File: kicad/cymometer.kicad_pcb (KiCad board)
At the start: 2 copper layers, 135.4 x 62 mm, 45 parts, among them IC1 74150, IC2 ATTINY2313-P, P1 BNC, P2 CONN_3X2, P3 CONN_10, P4 CONN_2, Q1 BC550, U1 74LS196, U2 74LS196, U3 74LS90, U4 74LS90, U5 7400, U6 74LS173, U7 7805, X1 127kHz

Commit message: Add new circuit
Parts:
- removed C13: CP1, Capacitors_ThroughHole:C_Radial_D8_L11.5_P3.5
- removed C14: CTRIM, Potentiometers:Potentiometer_Trimmer-Piher_PT15-V12-5_horizontal
- removed IC2: ATTINY2313-P, Housings_DIP:DIP-20_W7.62mm_LongPads
- removed U2: 74LS196, Housings_DIP:DIP-14_W7.62mm_LongPads
- removed U3, U4: 74LS90, Housings_DIP:DIP-14_W7.62mm_LongPads
- removed U5: 7400, Housings_DIP:DIP-14_W7.62mm_LongPads
- removed U6: 74LS173, Housings_DIP:DIP-16_W7.62mm_LongPads
- removed U7: 7805, Power_Integrations:TO-220
- added DD1: к531ие14, Housings_DIP:DIP-14_W7.62mm_LongPads, F.Cu at (84.1, 33.0)
- added DD2: к531ие14, Housings_DIP:DIP-14_W7.62mm_LongPads, F.Cu at (83.8, 68.1)
- added DD3: к155ла3, Housings_DIP:DIP-14_W7.62mm_LongPads, F.Cu at (38.5, 31.8)
- added DD4: кр1533кп7, Housings_DIP:DIP-16_W7.62mm_LongPads, F.Cu at (83.8, 51.0)
- added DD5: к155ир15, Housings_DIP:DIP-16_W7.62mm_LongPads, F.Cu at (56.9, 68.1)
- C1: value C -> 0.22; footprint Capacitors_ThroughHole:C_Disc_D12_P7.75 -> Capacitors_ThroughHole:C_Rect_L7_W2.5_P5
- C10, C11, C12, C7, C8, C9: value C -> 0.1; footprint Capacitors_ThroughHole:C_Disc_D12_P7.75 -> capacitors:C_Rect_L7_W2.5_P5
- C15: value C -> CTRIM; footprint Capacitors_ThroughHole:C_Disc_D12_P7.75 -> Potentiometers:Potentiometer_Trimmer-Piher_PT15-V12-5_horizontal
- C16: footprint Capacitors_ThroughHole:C_Disc_D12_P7.75 -> Capacitors_ThroughHole:C_Rect_L7_W2_P5
- C17: value CP1 -> C; footprint Capacitors_ThroughHole:C_Radial_D8_L21_P3.8 -> Capacitors_ThroughHole:C_Rect_L7_W2_P5
- C2: value C -> 100.0; footprint Capacitors_ThroughHole:C_Radial_D8_L13_P3.8 -> Capacitors_ThroughHole:C_Radial_D6.3_L11.2_P2.5
- C3: value C -> 680; footprint Capacitors_ThroughHole:C_Rect_L13_W4_P10 -> Capacitors_ThroughHole:C_Rect_L7_W3.5_P5
- C4: value CP1 -> 22.0; footprint Capacitors_ThroughHole:C_Radial_D8_L13_P3.8 -> Capacitors_ThroughHole:C_Radial_D6.3_L11.2_P2.5
- C5: value C -> 470.0; footprint Capacitors_ThroughHole:C_Disc_D12_P7.75 -> Capacitors_ThroughHole:C_Radial_D8_L21_P3.8
- C6: value C -> 100.0; footprint Capacitors_ThroughHole:C_Disc_D12_P7.75 -> Capacitors_ThroughHole:C_Radial_D6.3_L11.2_P2.5
- D1: value DIODE -> КД503А
- IC1: value 74150 -> ATTINY2313-P; footprint Housings_DIP:DIP-24_W15.24mm_LongPads -> Housings_DIP:DIP-20_W7.62mm_LongPads
- P1: footprint Connect:bornier2 -> Pin_Headers:Pin_Header_Straight_1x02
- P2: value CONN_3X2 -> CONN_2; footprint Socket_Strips:Socket_Strip_Straight_2x03 -> Pin_Headers:Pin_Header_Straight_1x02
- P3: value CONN_10 -> CONN_3X2; footprint Socket_Strips:Socket_Strip_Straight_1x10 -> Pin_Headers:Pin_Header_Straight_2x03
- P4: value CONN_2 -> CONN_12; footprint Connect:bornier2 -> Pin_Headers:Pin_Header_Straight_1x12
- R1: value R -> 10k
- R10: value R -> 510
- R2: value R -> 1k; footprint Resistors_ThroughHole:Resistor_Horizontal_RM25mm -> Resistors_ThroughHole:Resistor_Horizontal_RM10mm
- R3: value R -> 150k
- R4: value R -> 360
- R5: value R -> 100
- R6: value R -> 1k
- R7, R8: value R -> 2.2k
- R9: value R -> 47k
- RV1: value POT -> 1k
- U1: value 74LS196 -> 7805; footprint Housings_DIP:DIP-14_W7.62mm_LongPads -> Power_Integrations:TO-220
- X1: value 127kHz -> 16.000
- moved C8 97.4 mm to (35.1, 27.9), turned to 270 degrees
- moved P1 77.5 mm to (31.2, 71.4)
- moved C17 69.4 mm to (83.9, 23.7), turned to 270 degrees
- moved C1 69.2 mm to (31.4, 67.1), turned to 90 degrees
- moved D2 67.6 mm to (102.9, 80.0), turned to 0 degrees
- moved X1 61.6 mm to (75.2, 24.4), turned to 180 degrees
- moved P3 60.1 mm to (111.0, 26.9), turned to 0 degrees
- moved C16 59.2 mm to (66.3, 23.6), turned to 270 degrees
- moved C11 56.8 mm to (80.0, 78.5)
- moved C7 55.1 mm to (59.9, 71.9), turned to 270 degrees
- moved C5 51.3 mm to (104.3, 70.4), turned to 180 degrees
- moved C12 49.0 mm to (100.5, 36.4), turned to 180 degrees
- moved U1 48.6 mm to (95.2, 79.0)
- moved C15 44.7 mm to (102.2, 32.1), turned to 90 degrees
- moved IC1 43.2 mm to (96.7, 39.8), turned to 0 degrees
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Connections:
- C10 pad 1: +5V -> VCC
- C11 pad 1: +5V -> VCC
- C12 pad 1: +5V -> VCC
- C15 pad 1: Net-(C14-Pad1) -> Net-(C15-Pad1)
- C15 pad 2: GND -> Net-(C15-Pad2)
- C16 pad 1: Net-(C14-Pad2) -> Net-(C15-Pad1)
- C17 pad 1: Net-(C17-Pad1) -> Net-(C15-Pad2)
- C2 pad 1: GND -> Net-(C2-Pad1)
- C2 pad 2: Net-(C2-Pad2) -> GND
- C5 pad 1: +5V -> Net-(C5-Pad1)
- C6 pad 1: +5V -> VCC
- C7 pad 1: +5V -> GND
- C7 pad 2: GND -> VCC
- C8 pad 1: +5V -> VCC
- C9 pad 1: +5V -> VCC
- D2 pad 3: Net-(C17-Pad1) -> Net-(C5-Pad1)
- IC1 pad 10: Net-(IC1-Pad10) -> GND
- IC1 pad 12: GND -> Net-(IC1-Pad12)
- IC1 pad 20: Net-(IC1-Pad20) -> VCC
- IC1 pad 4: Net-(IC1-Pad4) -> Net-(C15-Pad1)
- IC1 pad 5: Net-(IC1-Pad5) -> Net-(C15-Pad2)
- IC1 pad 6: Net-(IC1-Pad6) -> Net-(DD5-Pad7)
- IC1 pad 7: Net-(IC1-Pad7) -> Net-(DD1-Pad13)
- IC1 pad 8: Net-(IC1-Pad8) -> Net-(DD2-Pad12)
- IC1 pad 9: GND -> Net-(IC1-Pad9)
- P2 pad 1: Net-(IC2-Pad18) -> Net-(D2-Pad4)
- P2 pad 2: +5V -> Net-(D2-Pad2)
- P3 pad 1: GND -> Net-(IC1-Pad18)
- P3 pad 2: +5V -> VCC
- P3 pad 3: Net-(IC2-Pad19) -> Net-(IC1-Pad19)
- P3 pad 4: Net-(IC2-Pad18) -> Net-(IC1-Pad17)
- P3 pad 5: Net-(IC2-Pad17) -> Net-(IC1-Pad1)
- P3 pad 6: Net-(IC2-Pad16) -> GND
- P4 pad 1: Net-(D2-Pad4) -> GND
- P4 pad 2: Net-(D2-Pad2) -> VCC
- Q1 pad 1: Net-(C2-Pad2) -> Net-(C2-Pad1)
- R1 pad 1: +5V -> Net-(C1-Pad2)
- R1 pad 2: Net-(R1-Pad2) -> Net-(D1-Pad2)
- R10 pad 1: +5V -> VCC
- R10 pad 2: Net-(R10-Pad2) -> Net-(DD1-Pad8)
- R2 pad 1: Net-(C1-Pad2) -> VCC
- R2 pad 2: Net-(D1-Pad2) -> Net-(DD1-Pad1)
- R3 pad 1: Net-(C2-Pad2) -> Net-(C2-Pad1)
- R5 pad 1: Net-(C2-Pad2) -> Net-(C2-Pad1)
- R5 pad 2: +5V -> VCC
- R7 pad 1: +5V -> VCC
- R8 pad 1: +5V -> VCC
- R9 pad 2: Net-(R10-Pad2) -> Net-(DD1-Pad8)
- RV1 pad 1: Net-(R6-Pad2) -> GND
- RV1 pad 3: GND -> Net-(R6-Pad2)
- U1 pad 1: Net-(R1-Pad2) -> Net-(C5-Pad1)
- U1 pad 2: Net-(IC1-Pad6) -> GND
- U1 pad 3: GND -> VCC
- X1 pad 1: Net-(C14-Pad2) -> Net-(C15-Pad2)
- X1 pad 2: Net-(C14-Pad1) -> Net-(C15-Pad1)
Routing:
- net +5V: track 391.6 -> 0.00 mm
- net VCC: track 0.00 -> 352.1 mm
- net GND: track 583.1 -> 420.9 mm
- net Net-(IC2-Pad7): track 148.2 -> 0.00 mm, vias 1 -> 0
- net Net-(IC2-Pad3): track 122.6 -> 0.00 mm, vias 2 -> 0
- net Net-(DD1-Pad12): track 0.00 -> 117.0 mm
- net Net-(IC1-Pad10): track 90.5 -> 0.00 mm
- net Net-(C15-Pad1): track 0.00 -> 88.7 mm
- net Net-(IC1-Pad7): track 86.6 -> 0.00 mm
- net Net-(IC1-Pad4): track 83.9 -> 0.00 mm
- net Net-(DD2-Pad12): track 0.00 -> 83.9 mm
- net Net-(IC1-Pad5): track 80.6 -> 0.00 mm, vias 1 -> 0
- net Net-(DD1-Pad13): track 0.00 -> 76.9 mm, vias 0 -> 1
- net Net-(U1-Pad13): track 69.7 -> 0.00 mm, vias 2 -> 0
- net Net-(IC1-Pad16): track 78.4 -> 9.45 mm
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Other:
- board size 135.4 x 62 mm -> 88.4 x 62 mm
- net class Default: clearance 0.7 -> 0.6
- rule trace_clearance: 0.7 -> 0.6
- board text added: "Cumometer"

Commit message: Add libraries
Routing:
- net Net-(DD1-Pad13): track 76.9 -> 59.7 mm
- net GND: track 420.9 -> 416.7 mm
- net Net-(DD3-Pad10): track 85.6 -> 81.6 mm
- net Net-(C15-Pad2): track 49.1 -> 46.8 mm
- net Net-(DD2-Pad2): track 29.6 -> 27.4 mm
- net Net-(DD5-Pad14): track 91.5 -> 93.6 mm
- net Net-(C15-Pad1): track 88.7 -> 86.8 mm
- net Net-(DD1-Pad12): track 117.0 -> 115.2 mm
- net Net-(DD2-Pad12): track 83.9 -> 85.7 mm
- net Net-(DD4-Pad9): track 26.7 -> 25.4 mm
- net Net-(DD2-Pad5): track 16.4 -> 15.2 mm
- net Net-(DD2-Pad9): track 27.2 -> 28.1 mm
- net Net-(DD1-Pad5): track 29.7 -> 28.8 mm
- net Net-(C5-Pad1): track 23.9 -> 23.2 mm
- net Net-(DD1-Pad9): track 14.1 -> 13.5 mm
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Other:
- board text added: "Cymometer"
- board text removed: "Cumometer"

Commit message: Add display board
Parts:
- added AFF1: 7SEGMENTS, cymometer:7segment_small, F.Cu at (155.0, 114.2)
- added AFF2: 7SEGMENTS, cymometer:7segment_small, F.Cu at (147.4, 114.2)
- added AFF3: 7SEGMENTS, cymometer:7segment_small, F.Cu at (139.8, 114.2)
- added AFF4: 7SEGMENTS, cymometer:7segment_small, F.Cu at (132.1, 114.2)
- added AFF5: 7SEGMENTS, cymometer:7segment_small, F.Cu at (124.5, 114.2)
- added AFF6: 7SEGMENTS, cymometer:7segment_small, F.Cu at (116.9, 114.2)
- added AFF7: 7SEGMENTS, cymometer:7segment_small, F.Cu at (109.3, 114.2)
- added AFF8: 7SEGMENTS, cymometer:7segment_small, F.Cu at (101.6, 114.3)
- added C13: C, cymometer:C_Rect_L7_W2.5_P5, B.Cu at (107.5, 132.2)
- added D4: LED, cymometer:LED, F.Cu at (96.5, 118.1)
- added D5: LED, cymometer:LED, F.Cu at (96.5, 110.5)
- added DD6: к155ид10, Housings_DIP:DIP-16_W7.62mm_LongPads, B.Cu at (111.0, 128.4)
- added DD7: 74HC595, Housings_DIP:DIP-16_W7.62mm_LongPads, B.Cu at (82.4, 128.4)
- added P5: CONN_12, Pin_Headers:Pin_Header_Straight_1x12, B.Cu at (168.6, 108.0)
- added R12: R, Resistors_ThroughHole:Resistor_Vertical_RM5mm, B.Cu at (104.1, 133.3)
- added R13: R, Resistors_ThroughHole:Resistor_Vertical_RM5mm, B.Cu at (83.8, 119.1)
- added R14: R, Resistors_ThroughHole:Resistor_Vertical_RM5mm, B.Cu at (87.1, 106.7)
- added R15: R, Resistors_ThroughHole:Resistor_Vertical_RM5mm, B.Cu at (86.4, 119.1)
- added R16: R, Resistors_ThroughHole:Resistor_Vertical_RM5mm, B.Cu at (89.0, 119.2)
- added R17: R, Resistors_ThroughHole:Resistor_Vertical_RM5mm, B.Cu at (91.6, 119.3)
- added R18: R, Resistors_ThroughHole:Resistor_Vertical_RM5mm, B.Cu at (87.1, 109.3)
- added R19: R, Resistors_ThroughHole:Resistor_Vertical_RM5mm, B.Cu at (87.0, 111.9)
- added SW1: SW_PUSH, Buttons_Switches_ThroughHole:SW_PUSH-12mm, F.Cu at (156.9, 131.0)
- added SW2: SW_PUSH, Buttons_Switches_ThroughHole:SW_PUSH-12mm, F.Cu at (140.1, 131.1)
- added SW3: SPST, Buttons_Switches_ThroughHole:SW_NKK_G1xJP, F.Cu at (163.1, 113.9)
- C10, C11, C12, C7, C8, C9: footprint capacitors:C_Rect_L7_W2.5_P5 -> cymometer:C_Rect_L7_W2.5_P5
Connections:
- R3 pad 1: Net-(C2-Pad1) -> (no net)
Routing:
- net Net-(DD7-Pad11): track 0.00 -> 160.0 mm
- net Net-(DD7-Pad12): track 0.00 -> 157.6 mm, vias 0 -> 3
- net VCC: track 352.0 -> 471.6 mm, vias 0 -> 1
- net Net-(DD7-Pad14): track 0.00 -> 94.8 mm
- net Net-(DD6-Pad15): track 0.00 -> 94.8 mm
- net Net-(AFF1-Pad4): track 0.00 -> 93.9 mm
- net Net-(AFF1-Pad7): track 0.00 -> 91.7 mm
- net GND: track 416.7 -> 506.2 mm
- net Net-(AFF1-Pad6): track 0.00 -> 86.1 mm
- net Net-(AFF1-Pad2): track 0.00 -> 84.5 mm
- net Net-(DD6-Pad14): track 0.00 -> 80.6 mm
- net Net-(AFF1-Pad9): track 0.00 -> 78.8 mm
- net Net-(AFF1-Pad10): track 0.00 -> 77.3 mm
- net Net-(AFF1-Pad1): track 0.00 -> 77.1 mm
- net Net-(AFF1-Pad5): track 0.00 -> 65.2 mm
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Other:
- board size 88.4 x 62 mm -> 143 x 118.6 mm

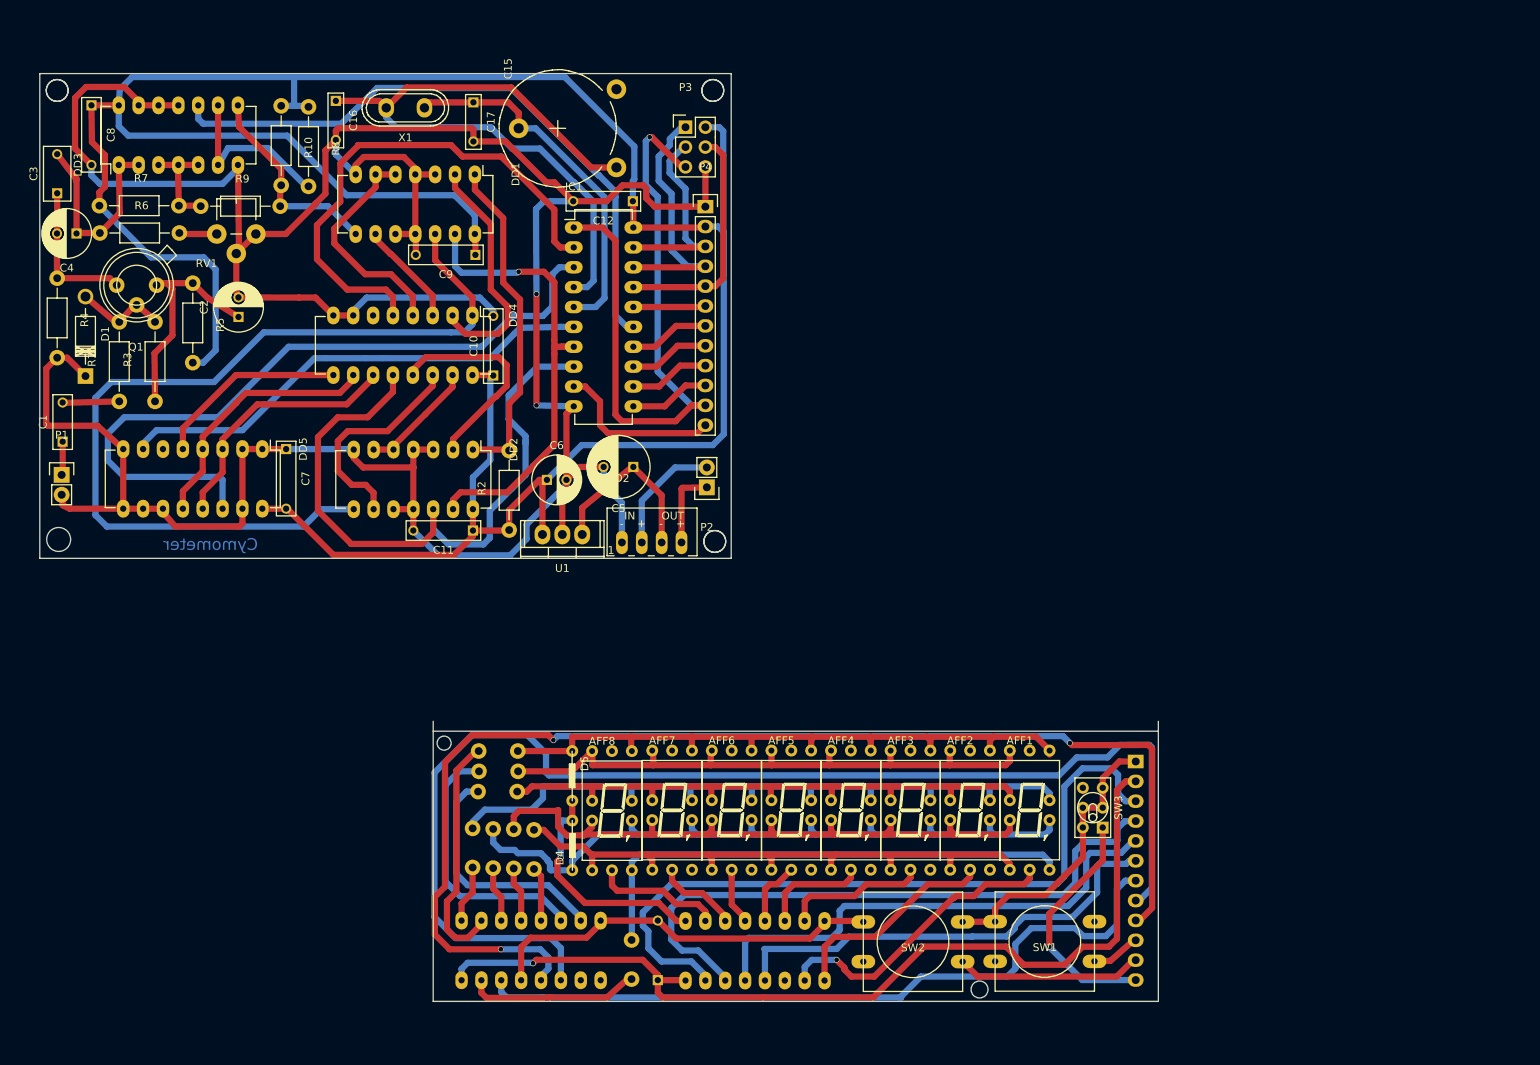
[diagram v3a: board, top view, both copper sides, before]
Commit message: Modified circuit for Atmega8-p
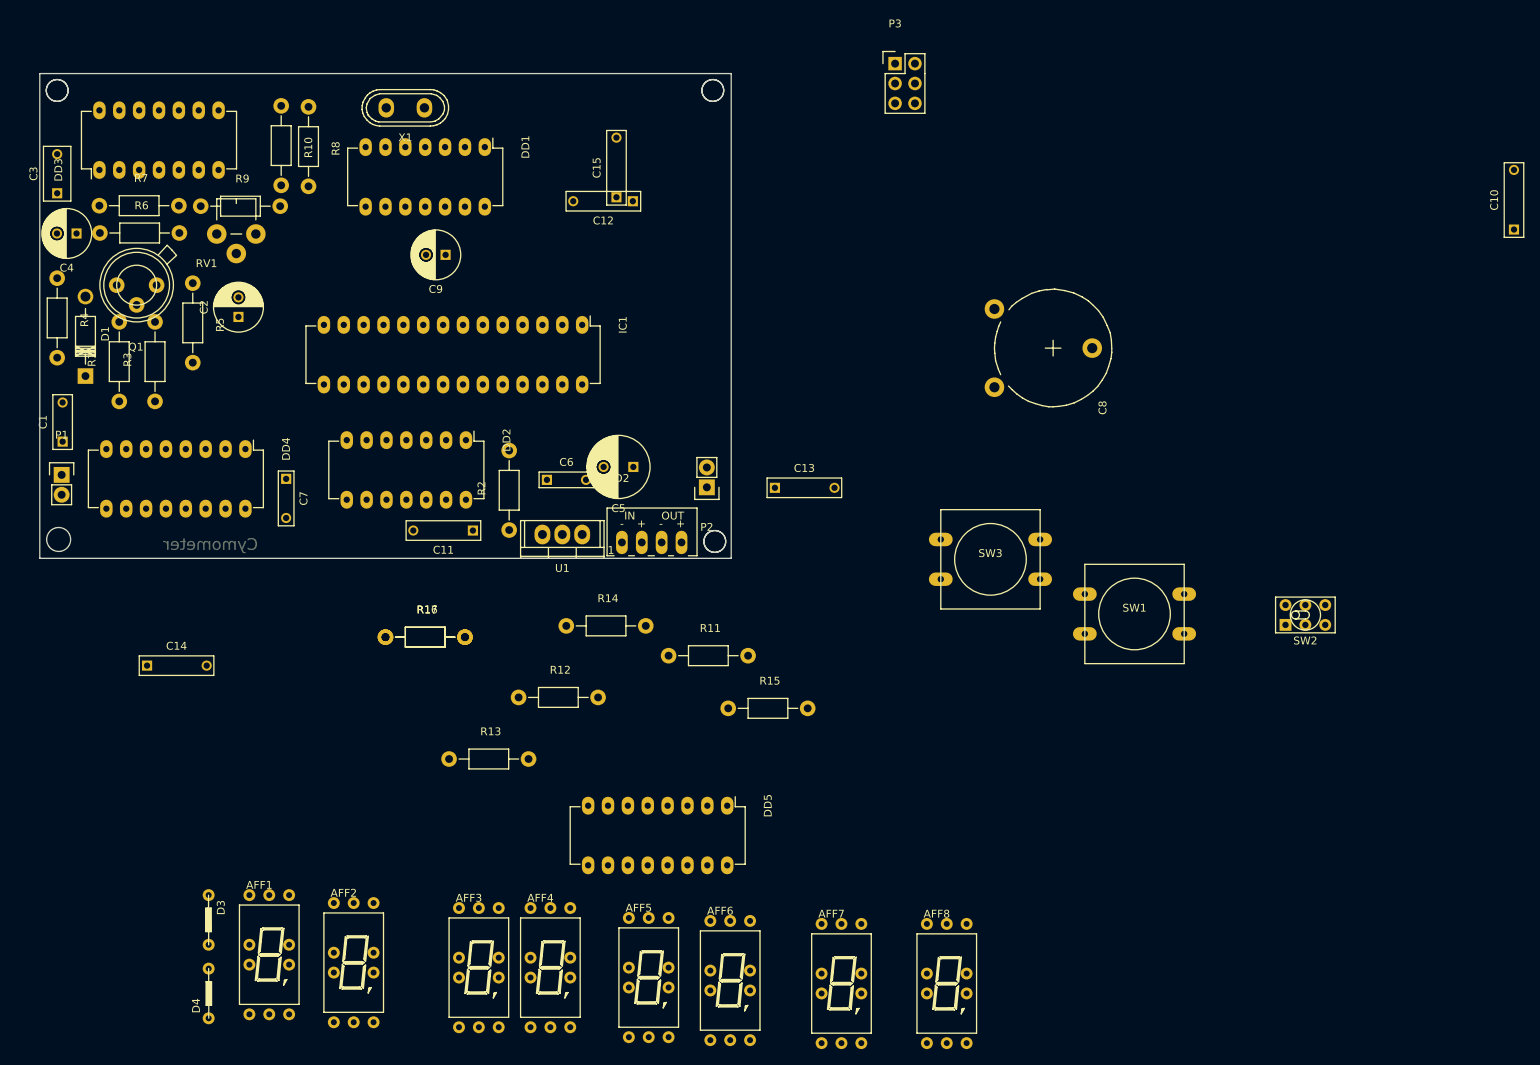
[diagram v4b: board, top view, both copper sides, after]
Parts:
- removed C16, C17: C, Capacitors_ThroughHole:C_Rect_L7_W2_P5
- removed D5: LED, cymometer:LED
- removed DD6: к155ид10, Housings_DIP:DIP-16_W7.62mm_LongPads
- removed DD7: 74HC595, Housings_DIP:DIP-16_W7.62mm_LongPads
- removed P4, P5: CONN_12, Pin_Headers:Pin_Header_Straight_1x12
- removed R18, R19: R, Resistors_ThroughHole:Resistor_Vertical_RM5mm
- added C14: 0.1, cymometer:C_Rect_L7_W2.5_P5, F.Cu at (46.0, 95.8)
- added D3: LED, cymometer:LED, F.Cu at (50.0, 128.9)
- added R11: R, Resistors_ThroughHole:Resistor_Horizontal_RM10mm, F.Cu at (108.8, 94.5)
- C13: value C -> 0.1; moved to F.Cu
- C15: value CTRIM -> 0.1; footprint Potentiometers:Potentiometer_Trimmer-Piher_PT15-V12-5_horizontal -> cymometer:C_Rect_L7_W2.5_P5
- C6: value 100.0 -> C; footprint Capacitors_ThroughHole:C_Radial_D6.3_L11.2_P2.5 -> Capacitors_ThroughHole:C_Rect_L7_W2_P5
- C7: value 0.1 -> C; footprint cymometer:C_Rect_L7_W2.5_P5 -> Capacitors_ThroughHole:C_Rect_L7_W2_P5
- C8: value 0.1 -> CTRIM; footprint cymometer:C_Rect_L7_W2.5_P5 -> Potentiometers:Potentiometer_Trimmer-Piher_PT15-V12-5_horizontal
- C9: value 0.1 -> 100.0; footprint cymometer:C_Rect_L7_W2.5_P5 -> Capacitors_ThroughHole:C_Radial_D6.3_L11.2_P2.5
- DD5: value к155ир15 -> к155ид10
- IC1: value ATTINY2313-P -> ATMEGA8-P; footprint Housings_DIP:DIP-20_W7.62mm_LongPads -> Housings_DIP:DIP-28_W7.62mm_LongPads
- R12, R13, R14, R15, R16, R17: footprint Resistors_ThroughHole:Resistor_Vertical_RM5mm -> Resistors_ThroughHole:Resistor_Horizontal_RM10mm; moved to F.Cu
- R8: value 2.2k -> 47k
- R9: value 47k -> 2.2k
- SW2: value SW_PUSH -> SPST; footprint Buttons_Switches_ThroughHole:SW_PUSH-12mm -> Buttons_Switches_ThroughHole:SW_NKK_G1xJP
- SW3: value SPST -> SW_PUSH; footprint Buttons_Switches_ThroughHole:SW_NKK_G1xJP -> Buttons_Switches_ThroughHole:SW_PUSH-12mm
- X1: value 16.000 -> 20.48 MГц
- moved C10 131.8 mm to (216.9, 36.2)
- moved C8 117.6 mm to (150.5, 50.2)
- moved AFF1 99.0 mm to (57.8, 132.7)
- moved AFF2 81.2 mm to (68.6, 133.7)
- moved DD5 74.9 mm to (116.3, 113.7)
- moved SW2 65.3 mm to (190.2, 89.3), turned to 0 degrees
- moved C13 62.0 mm to (126.2, 73.0), turned to 0 degrees
- moved AFF3 58.7 mm to (84.6, 134.4)
- moved D4 50.2 mm to (50.0, 137.0)
- moved AFF8 48.2 mm to (144.4, 136.4)
- moved SW1 43.4 mm to (168.4, 89.2), turned to 0 degrees
- moved AFF4 43.4 mm to (93.7, 134.4)
- moved R12 36.5 mm to (89.7, 99.8), turned to 0 degrees
- moved R15 35.0 mm to (116.5, 101.2), turned to 0 degrees
- moved SW3 34.3 mm to (150.0, 82.2), turned to 0 degrees
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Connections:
- AFF1 pad 5: Net-(AFF1-Pad5) -> (no net)
- AFF2 pad 3: Net-(AFF2-Pad3) -> (no net)
- AFF2 pad 5: Net-(AFF1-Pad5) -> (no net)
- AFF2 pad 8: (no net) -> Net-(AFF2-Pad8)
- AFF3 pad 5: Net-(AFF1-Pad5) -> (no net)
- AFF4 pad 5: Net-(AFF1-Pad5) -> (no net)
- AFF5 pad 5: Net-(AFF1-Pad5) -> (no net)
- AFF6 pad 5: Net-(AFF1-Pad5) -> (no net)
- AFF7 pad 5: Net-(AFF1-Pad5) -> (no net)
- AFF8 pad 5: Net-(AFF1-Pad5) -> (no net)
- C10 pad 1: VCC -> GND
- C10 pad 2: GND -> VCC
- C15 pad 1: Net-(C15-Pad1) -> VCC
- C15 pad 2: Net-(C15-Pad2) -> GND
- C6 pad 1: VCC -> Net-(C6-Pad1)
- C7 pad 1: GND -> Net-(C7-Pad1)
- C7 pad 2: VCC -> GND
- C8 pad 1: VCC -> Net-(C6-Pad1)
- C8 pad 2: GND -> Net-(C7-Pad1)
- D4 pad 2: Net-(D4-Pad2) -> Net-(D3-Pad2)
- DD5 pad 1: GND -> Net-(D3-Pad2)
- DD5 pad 10: GND -> Net-(AFF1-Pad3)
- DD5 pad 11: GND -> (no net)
- DD5 pad 12: Net-(DD4-Pad10) -> Net-(DD5-Pad12)
- DD5 pad 13: Net-(DD4-Pad11) -> Net-(DD5-Pad13)
- DD5 pad 15: GND -> Net-(DD5-Pad15)
- DD5 pad 2: GND -> Net-(AFF8-Pad3)
- DD5 pad 3: Net-(DD4-Pad11) -> Net-(AFF7-Pad3)
- DD5 pad 4: Net-(DD4-Pad10) -> Net-(AFF6-Pad3)
- DD5 pad 5: Net-(DD4-Pad9) -> Net-(AFF5-Pad3)
- DD5 pad 6: (no net) -> Net-(AFF4-Pad3)
- DD5 pad 7: Net-(DD5-Pad7) -> Net-(AFF3-Pad3)
- DD5 pad 9: GND -> Net-(AFF2-Pad8)
- IC1 pad 10: GND -> Net-(C7-Pad1)
- IC1 pad 11: Net-(IC1-Pad11) -> Net-(DD4-Pad11)
- IC1 pad 12: Net-(IC1-Pad12) -> Net-(DD4-Pad10)
- IC1 pad 13: Net-(IC1-Pad13) -> Net-(DD4-Pad9)
- IC1 pad 14: Net-(IC1-Pad14) -> Net-(DD1-Pad13)
- IC1 pad 16: Net-(IC1-Pad16) -> Net-(DD4-Pad5)
- IC1 pad 2: Net-(DD4-Pad5) -> Net-(DD5-Pad15)
- IC1 pad 20: VCC -> (no net)
- IC1 pad 4: Net-(C15-Pad1) -> Net-(DD5-Pad13)
- IC1 pad 5: Net-(C15-Pad2) -> Net-(DD5-Pad12)
- IC1 pad 6: Net-(DD5-Pad7) -> Net-(DD2-Pad12)
- IC1 pad 7: Net-(DD1-Pad13) -> VCC
- IC1 pad 8: Net-(DD2-Pad12) -> GND
- IC1 pad 9: Net-(IC1-Pad9) -> Net-(C6-Pad1)
- R12 pad 1: Net-(AFF1-Pad5) -> Net-(AFF1-Pad6)
- R12 pad 2: Net-(DD7-Pad15) -> Net-(IC1-Pad23)
- R13 pad 1: Net-(AFF1-Pad7) -> Net-(AFF1-Pad4)
- R13 pad 2: Net-(DD7-Pad1) -> Net-(IC1-Pad24)
- R14 pad 1: Net-(AFF1-Pad6) -> Net-(AFF1-Pad2)
- R14 pad 2: Net-(DD7-Pad2) -> Net-(IC1-Pad25)
- R15 pad 1: Net-(AFF1-Pad4) -> Net-(AFF1-Pad1)
- R15 pad 2: Net-(DD7-Pad3) -> Net-(IC1-Pad26)
- R16 pad 1: Net-(AFF1-Pad2) -> Net-(AFF1-Pad9)
- R16 pad 2: Net-(DD7-Pad4) -> Net-(IC1-Pad27)
- R17 pad 1: Net-(AFF1-Pad1) -> Net-(AFF1-Pad10)
- R17 pad 2: Net-(DD7-Pad5) -> Net-(IC1-Pad28)
- R8 pad 1: VCC -> Net-(DD3-Pad3)
- R8 pad 2: Net-(DD3-Pad6) -> Net-(DD1-Pad8)
- R9 pad 1: Net-(DD3-Pad3) -> VCC
- R9 pad 2: Net-(DD1-Pad8) -> Net-(DD3-Pad6)
- SW1 pad 1: Net-(P5-Pad10) -> Net-(IC1-Pad18)
- SW2 pad 1: Net-(P5-Pad11) -> Net-(IC1-Pad17)
- SW3 pad 1: Net-(P5-Pad12) -> Net-(IC1-Pad1)
- X1 pad 1: Net-(C15-Pad2) -> Net-(C7-Pad1)
- X1 pad 2: Net-(C15-Pad1) -> Net-(C6-Pad1)
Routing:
- net GND: track 506.2 -> 0.00 mm, vias 2 -> 0
- net VCC: track 471.6 -> 0.00 mm, vias 1 -> 0
- net Net-(DD7-Pad11): track 160.0 -> 0.00 mm
- net Net-(DD7-Pad12): track 157.6 -> 0.00 mm, vias 3 -> 0
- net Net-(DD1-Pad12): track 115.2 -> 0.00 mm
- net Net-(DD7-Pad14): track 94.8 -> 0.00 mm
- net Net-(DD6-Pad15): track 94.8 -> 0.00 mm
- net Net-(AFF1-Pad4): track 93.9 -> 0.00 mm
- net Net-(DD5-Pad14): track 93.6 -> 0.00 mm
- net Net-(AFF1-Pad7): track 91.7 -> 0.00 mm
- net Net-(C15-Pad1): track 86.8 -> 0.00 mm
- net Net-(AFF1-Pad6): track 86.1 -> 0.00 mm
- net Net-(IC1-Pad1): track 86.0 -> 0.00 mm, vias 1 -> 0
- net Net-(DD2-Pad12): track 85.7 -> 0.00 mm
- net Net-(AFF1-Pad2): track 84.5 -> 0.00 mm
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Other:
- board size 143 x 118.6 mm -> 88.4 x 62 mm
